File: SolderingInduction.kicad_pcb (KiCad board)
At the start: 4 copper layers, 68.9 x 37.6 mm, 57 parts, among them J1 MC-307, J3 RBP_GPIO_CONN, SW1 SW_Push, SW2 SW_Push, SW3 SW_Push, SW4 SW_Push, SW5 SW_Push, SW6 SW_Push, SW7 SW_Push, SW8 SW_Push, U1 SPX2920M3-3.3_SOT223, U3 W25Q32JVZP, U4 RP2040, Y1 X322512MMB4SI

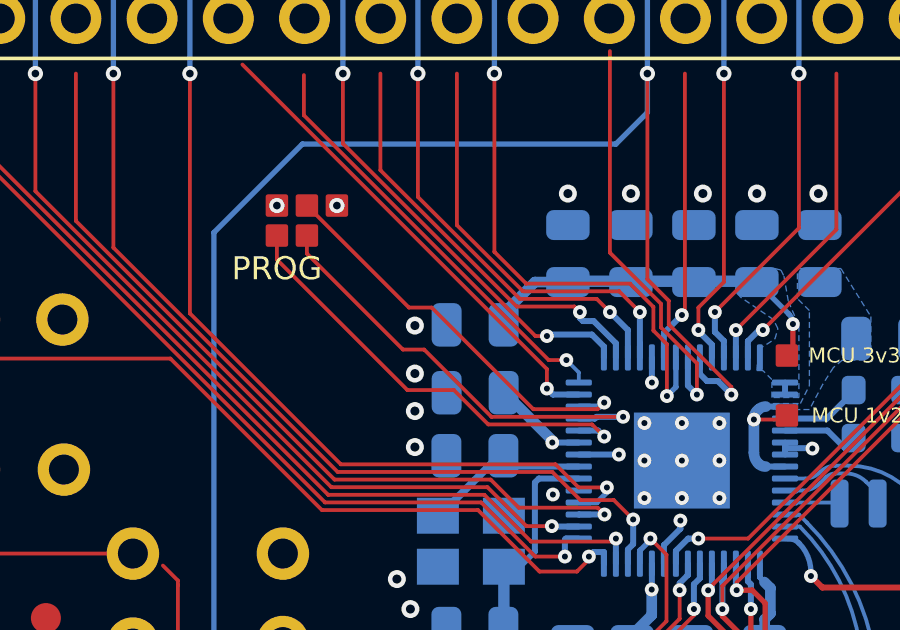
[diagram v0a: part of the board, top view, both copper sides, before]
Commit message: Grouping GPIO bus to avoid split grounds
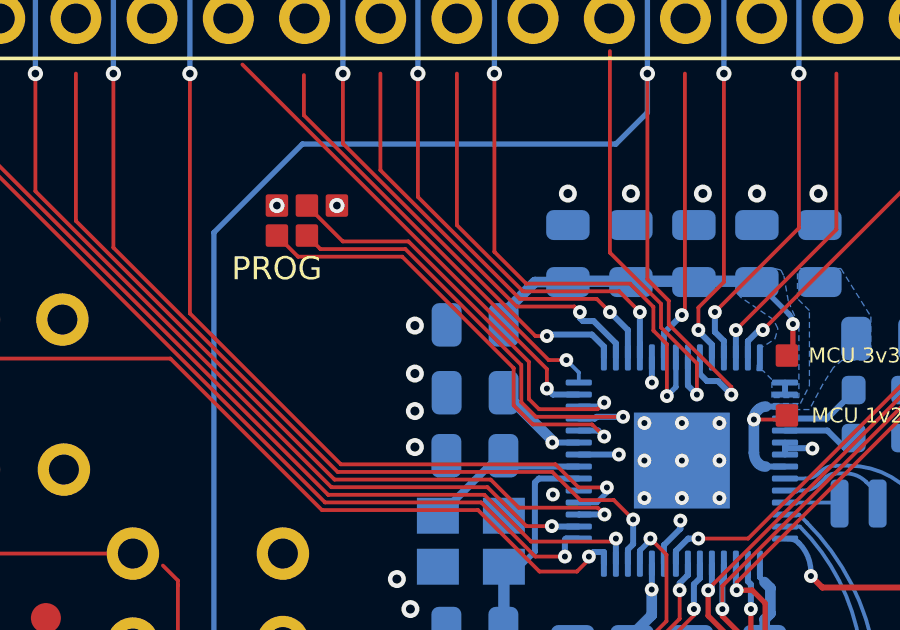
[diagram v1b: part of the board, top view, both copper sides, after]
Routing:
- net Net-(U4-Pad26): track 13.7 -> 14.4 mm
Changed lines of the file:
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@@
   (arc (start 152.4 62.480762) (mid 152.56893 63.330027) (end 153.05 64.05) (width 1) (layer "F.Cu") (net 27))
   (arc (start 153.05 64.05) (mid 153.901125 65.323798) (end 154.2 66.826345) (width 1) (layer "F.Cu") (net 27))
+  (segment (start 122.188988 73.288183) (end 120.238183 73.288183) (width 0.127) (layer "F.Cu") (net 29))
+  (segment (start 120.238183 73.288183) (end 119.9 72.95) (width 0.127) (layer "F.Cu") (net 29))
+  (segment (start 113.696 67.696) (end 112.5 66.5) (width 0.127) (layer "F.Cu") (net 29))
+  (segment (start 115.88679 67.696) (end 113.696 67.696) (width 0.127) (layer "F.Cu") (net 29))
+  (segment (start 119.9 72.95) (end 119.9 71.70921) (width 0.127) (layer "F.Cu") (net 29))
   (segment (start 122.409987 73.067184) (end 122.188988 73.288183) (width 0.127) (layer "F.Cu") (net 29))
-  (segment (start 122.188988 73.288183) (end 120.047393 73.288183) (width 0.127) (layer "F.Cu") (net 29))
-  (segment (start 115.9 69.9) (end 112.5 66.5) (width 0.127) (layer "F.Cu") (net 29))
-  (segment (start 116.65921 69.9) (end 115.9 69.9) (width 0.127) (layer "F.Cu") (net 29))
-  (segment (start 120.047393 73.288183) (end 116.65921 69.9) (width 0.127) (layer "F.Cu") (net 29))
+  (segment (start 119.9 71.70921) (end 115.88679 67.696) (width 0.127) (layer "F.Cu") (net 29))
   (via (at 122.409987 73.067184) (size 0.46) (drill 0.2) (layers "F.Cu" "B.Cu") (free) (net 29))
   (segment (start 121.562504 73.199997) (end 122.27717 73.200001) (width 0.2) (layer "B.Cu") (net 29))
   (segment (start 122.27717 73.200001) (end 122.409987 73.067184) (width 0.2) (layer "B.Cu") (net 29))
+  (segment (start 111.5 67.5) (end 112.204 68.204) (width 0.127) (layer "F.Cu") (net 30))
+  (segment (start 120.027763 73.796183) (end 122.00617 73.796183) (width 0.127) (layer "F.Cu") (net 30))
+  (segment (start 112.204 68.204) (end 115.67637 68.204) (width 0.127) (layer "F.Cu") (net 30))
+  (segment (start 119.392 71.91963) (end 119.392 73.16042) (width 0.127) (layer "F.Cu") (net 30))
+  (segment (start 115.67637 68.204) (end 119.392 71.91963) (width 0.127) (layer "F.Cu") (net 30))
   (segment (start 122.00617 73.796183) (end 122.409987 74.2) (width 0.127) (layer "F.Cu") (net 30))
-  (segment (start 115.85 72.65) (end 117.4 72.65) (width 0.127) (layer "F.Cu") (net 30))
-  (segment (start 111.5 68.3) (end 115.85 72.65) (width 0.127) (layer "F.Cu") (net 30))
-  (segment (start 117.4 72.65) (end 118.546183 73.796183) (width 0.127) (layer "F.Cu") (net 30))
-  (segment (start 118.546183 73.796183) (end 122.00617 73.796183) (width 0.127) (layer "F.Cu") (net 30))
-  (segment (start 111.5 67.5) (end 111.5 68.3) (width 0.127) (layer "F.Cu") (net 30))
+  (segment (start 119.392 73.16042) (end 120.027763 73.796183) (width 0.127) (layer "F.Cu") (net 30))
   (via (at 122.409987 74.2) (size 0.46) (drill 0.2) (layers "F.Cu" "B.Cu") (free) (net 30))
   (segment (start 122.209986 73.999999) (end 121.562505 73.999999) (width 0.2) (layer "B.Cu") (net 30))
   (segment (start 122.409987 74.2) (end 122.209986 73.999999) (width 0.2) (layer "B.Cu") (net 30))
-  (segment (start 116.40921 71.3) (end 115.7 71.3) (width 0.127) (layer "F.Cu") (net 31))
-  (segment (start 123.039988 73.542183) (end 118.651393 73.542183) (width 0.127) (layer "F.Cu") (net 31))
-  (segment (start 115.7 71.3) (end 112.5 68.1) (width 0.127) (layer "F.Cu") (net 31))
-  (segment (start 118.651393 73.542183) (end 116.40921 71.3) (width 0.127) (layer "F.Cu") (net 31))
-  (segment (start 112.5 68.1) (end 112.5 67.5) (width 0.127) (layer "F.Cu") (net 31))
+  (segment (start 119.646 71.81442) (end 115.78158 67.95) (width 0.127) (layer "F.Cu") (net 31))
+  (segment (start 112.95 67.95) (end 112.5 67.5) (width 0.127) (layer "F.Cu") (net 31))
+  (segment (start 123.039988 73.542183) (end 120.132973 73.542183) (width 0.127) (layer "F.Cu") (net 31))
+  (segment (start 115.78158 67.95) (end 112.95 67.95) (width 0.127) (layer "F.Cu") (net 31))
+  (segment (start 119.646 73.05521) (end 119.646 71.81442) (width 0.127) (layer "F.Cu") (net 31))
+  (segment (start 120.132973 73.542183) (end 119.646 73.05521) (width 0.127) (layer "F.Cu") (net 31))
   (via (at 123.039988 73.542183) (size 0.46) (drill 0.2) (layers "F.Cu" "B.Cu") (free) (net 31))
   (segment (start 122.097169 73.6) (end 121.562504 73.599999) (width 0.2) (layer "B.Cu") (net 31))

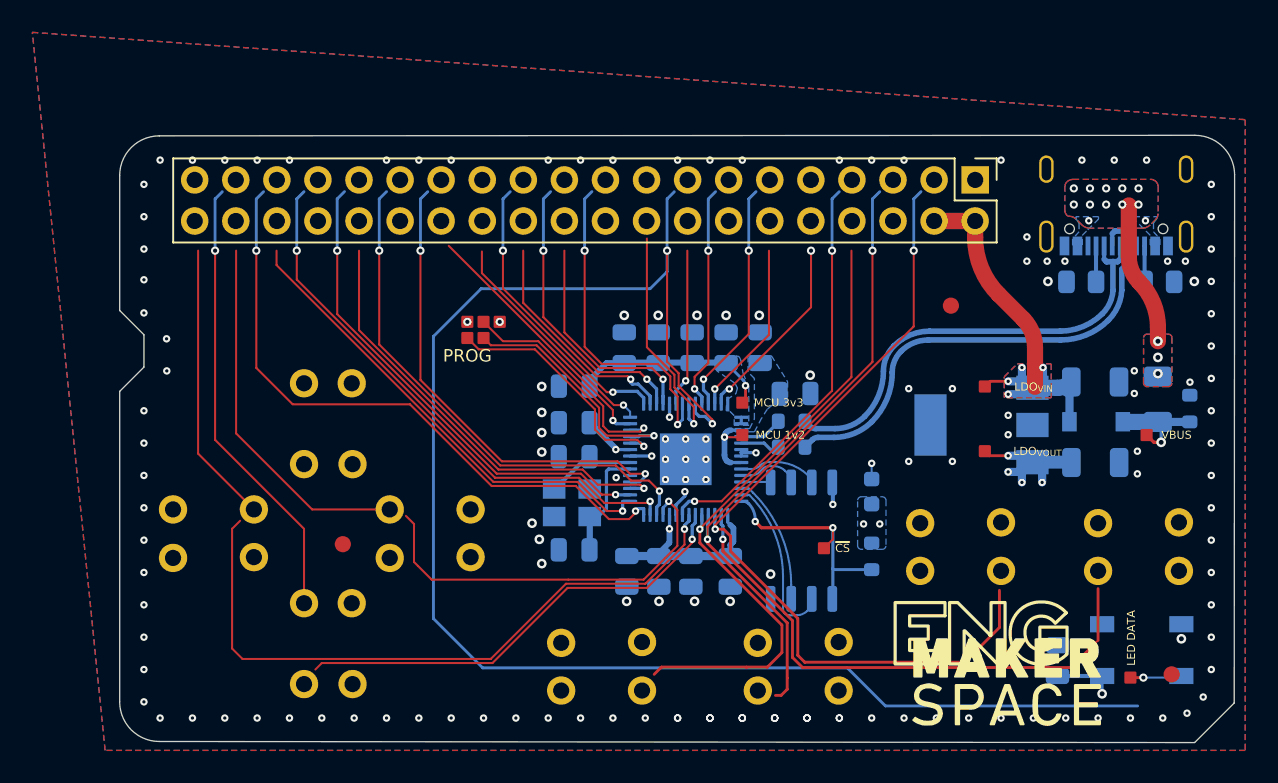
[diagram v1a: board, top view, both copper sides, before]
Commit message: Button Sch mapping + Silkscreen cleanup
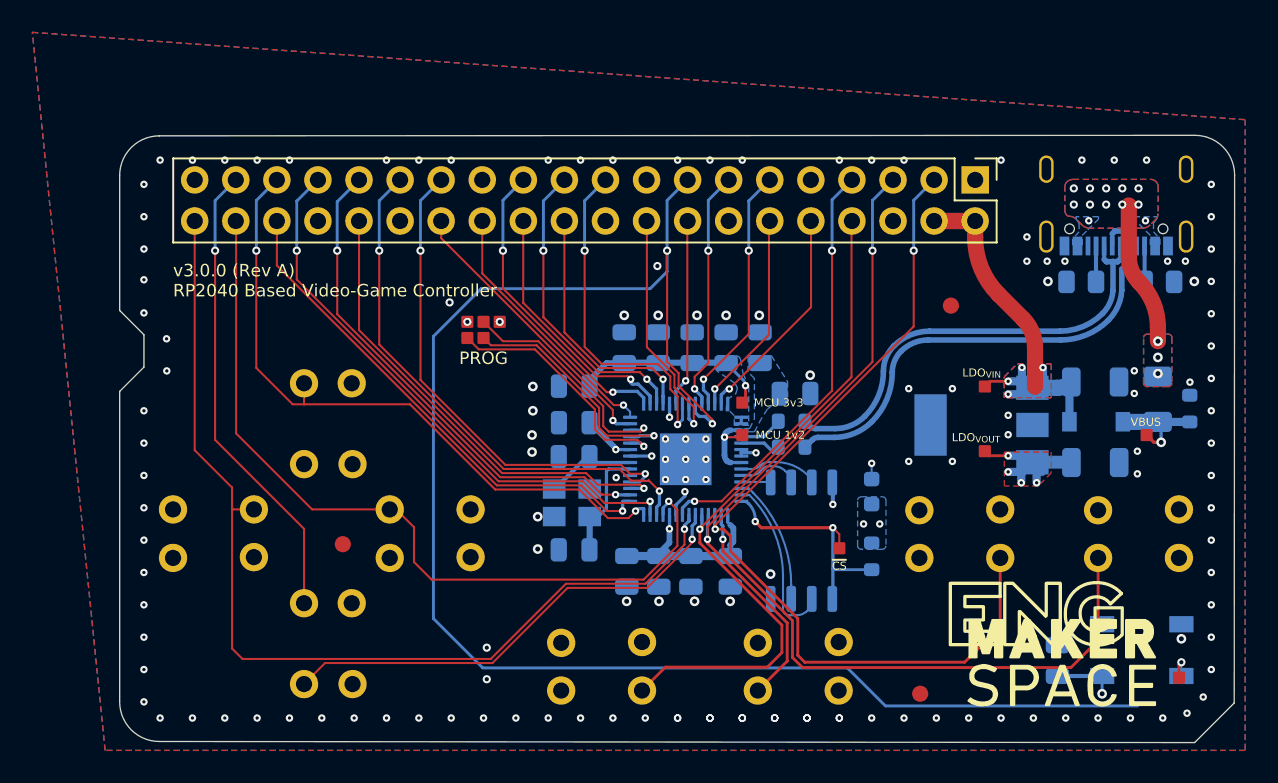
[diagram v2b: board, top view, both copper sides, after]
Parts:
- moved FID2 15.6 mm to (139.5, 89.5)
- moved REF** 3.61 mm to (141.4, 82.7)
- moved TP5 3.00 mm to (155.5, 88.5)
- moved TP12 0.95 mm to (134.5, 80.5)
- moved SW4 0.80 mm to (141.9, 79.6)
- moved SW6 0.80 mm to (153.0, 79.6)
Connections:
- J3 pad 11: /GPIO[17] -> /$.GPIO27
- J3 pad 12: /$.GPIO23 -> /GPIO[18]/PCM.CLK
- J3 pad 13: /GPIO[27] -> /$.GPIO26
- J3 pad 15: /GPIO[22] -> /$.GPIO25
- J3 pad 16: /GPIO[23] -> /$.GPIO22
- J3 pad 18: /GPIO[24] -> /$.GPIO24
- J3 pad 19: /GPIO[10]/SPI0.MOSI -> /$.GPIO23
- J3 pad 21: /GPIO[9]/SPI0.MISO -> /$.GPIO20
- J3 pad 22: /GPIO[25] -> /$.GPIO21
- J3 pad 23: /$.GPIO21 -> /$.GPIO18
- J3 pad 24: /GPIO[8]/SPI0.CE0 -> /$.GPIO19
- J3 pad 26: /GPIO[7]/SPI0.CE1 -> /$.GPIO17
- J3 pad 27: unconnected-(J3-Pad27) -> /$.GPIO15
- J3 pad 28: unconnected-(J3-Pad28) -> /$.GPIO16
- J3 pad 29: /GPIO[5] -> /$.GPIO9
- J3 pad 3: /GPIO[2]/SDA1 -> /$.GPIO1
- J3 pad 31: /GPIO[6] -> /$.GPIO13
- J3 pad 32: /GPIO[12]/PWM0 -> /$.GPIO14
- J3 pad 33: /$.GPIO20 -> /$.GPIO10
- J3 pad 35: /GPIO[19]/PCM.FS -> /$.GPIO11
- J3 pad 36: /GPIO[16] -> /$.GPIO12
- J3 pad 37: /GPIO[26] -> /$.GPIO4
- J3 pad 38: /$.GPIO24 -> /$.GPIO8
- J3 pad 40: /GPIO[21]/PCM.DOUT -> /$.GPIO5
- J3 pad 5: /GPIO[3]/SCL1 -> /$.GPIO2
- J3 pad 7: /$.GPIO22 -> /$.GPIO6
- J3 pad 8: /GPIO[14]/TXD0 -> /$.GPIO3
- SW1 pad 2: /BUTTON_LEFT -> /$.GPIO4
- SW2 pad 2: /BUTTON_UP -> /$.GPIO2
- SW3 pad 2: /BUTTON_DOWN -> /$.GPIO5
- SW4 pad 2: /BUTTON_RIGHT -> /$.GPIO1
- SW5 pad 2: /BUTTON_SELECT -> /$.GPIO11
- SW6 pad 2: /BUTTON_START -> /$.GPIO0
- SW7 pad 2: /BUTTON_A -> /$.GPIO8
- SW8 pad 2: /BUTTON_B -> /$.GPIO3
- U4 pad 40: /$.GPIO28 -> /GPIO[18]/PCM.CLK
- U4 pad 41: /$.GPIO29 -> /GPIO[15]/RXD0
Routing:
- net /$.GPIO4: track 28.4 -> 58.4 mm, vias 1 -> 2
- net /BUTTON_LEFT: track 27.9 -> 0.00 mm, vias 1 -> 0
- net /$.GPIO8: track 24.5 -> 50.2 mm
- net /BUTTON_A: track 22.7 -> 0.00 mm
- net /$.GPIO5: track 41.2 -> 63.2 mm
- net /BUTTON_DOWN: track 17.4 -> 0.00 mm
- net /GPIO[15]/RXD0: track 0.00 -> 13.7 mm, vias 0 -> 1
- net /GPIO[18]/PCM.CLK: track 0.00 -> 12.9 mm, vias 0 -> 1
- net /$.GPIO29: track 11.8 -> 0.00 mm, vias 2 -> 0
- net /$.GPIO28: track 10.9 -> 0.00 mm, vias 1 -> 0
- net /$.GPIO1: track 53.1 -> 56.2 mm
- net /$.GPIO3: track 40.2 -> 43.2 mm
- net /$.GPIO11: track 39.6 -> 41.9 mm
- net /$.GPIO0: track 33.7 -> 35.6 mm
- net /$.GPIO17: track 14.4 -> 16.3 mm
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- added copper zone on F.Cu, net +3V3
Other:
- board text added: "v3.0.0 (Rev A) RP2040 Based Video-Game Controller"

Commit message: Frog
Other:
- board text added: "making.unsw.edu.au"
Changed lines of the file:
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@@
   (gr_line (start 92.45 92.45) (end 156.467588 92.517588) (layer "Edge.Cuts") (width 0.01))
   (gr_line (start 158.917588 90.067588) (end 158.942588 57.417588) (layer "Edge.Cuts") (width 0.01))
-  (gr_text "v3.0.0 (Rev A)\nRP2040 Based Video-Game Controller" (at 93.3 63.95) (layer "F.SilkS")
-    (effects (font (size 0.77 0.77) (thickness 0.1925)) (justify left))
+  (gr_text "v3.0.0 (Rev A)\nRP2040 Based Video-Game Controller" (at 93.1 63.65) (layer "F.SilkS")
+    (effects (font (size 0.5 0.5) (thickness 0.125)) (justify left))
+  )
+  (gr_text "making.unsw.edu.au" (at 93.15 65.6) (layer "F.SilkS")
+    (effects (font (size 0.5 0.5) (thickness 0.125)) (justify left))
   )
   (gr_text "PROG" (at 112.5 68.75) (layer "F.SilkS")
-    (effects (font (size 0.77 0.77) (thickness 0.15)))
+    (effects (font (size 0.5 0.5) (thickness 0.125)))
   )
   (gr_text "Todo:\n* Tune DRC \n	- Ensure the scripted DRC cons don't conflict \n	- soldermask expansion \n	- silkscreen reqs \n	- trace clearances \n* Tune and run ERC\n* Clean up trace width / clearances\n* Clean up board dimensions \n* Confirm testpoints to 1mm spacing grid\n* Adjust all via sizes \n* Update schematic to 1117-3v3 \n* Redo power layout \n* Cleanup 3v3 and 1v2 power traces \n* Clean up zones \n* Clean up schematic \n* Route GPIO \n* Double check LED \n* Check if buttons can be diagonalized \n* Clean up D-pad layout\n* Clean up SWD footprint \n* check optimality of via placements \n* Draw out grid for vias \n* run traces to fan-in fan-out \n* Check clearances and trace widths \n* Check ground flow paths \n* Check button footprints \n* Check river routing consistency \n* Check USB interface layout \n* Clean up silkscreen \n* Change QR code\n* Clean up oscillator \n* Clean up passives \n* Ensure all decoupling caps grounded properly \n* Map GPIO \n* Connect up GPIO \n* Check accessibility \n* Comply with JLC SMT reqs" (at 166.8 69.9352) (layer "Cmts.User")
